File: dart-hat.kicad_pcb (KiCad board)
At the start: 2 copper layers, 85 x 56 mm, 119 parts, among them IC1 PCA9615DPJ, J0 XT60 Female, J1 Raspberry_Pi_2_3, J2 CAN_CON, J3 SM07B-SRSS-TBLFSN, M1 Motor_Servo, M2 Motor_Servo, M3 Motor_Servo, M4 Motor_Servo, Q1 Q_PMOS_DSG, Q2 Q_PMOS_DSG, Q3 DMMT5401, U1 CAT24C32YI-GT3, U2 MCP2515-xSO, U3 MCP2551-I-SN, U4 LM2677S-5.0, U5 BMI088, U6 PCA9685PW, U7 LM2677S-5.0, U8 LM2677S-3.3, Y1 16MHz

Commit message: [schematic] fix 3v3 symbol pin to use 3v3_pi instead of 5V_SRV
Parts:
- C10, C19, C2, C20, C3, C9, IC1, JP1, JP4, JP6, R15, R16, R18, R19, R20, R21, R22, R4, R5, R6, R7, R8, U1, U6: moved to B.Cu
- CP1, CP21: value 1000uF -> 330uF; footprint EEE-TP1J102M:CAP_EEETP1J102M -> Capacitor_THT:CP_Radial_D10.0mm_P5.00mm
- D5: value D_Schottky -> D_Schottky_KKA
- Q2: footprint Package_TO_SOT_SMD:TO-263-3_TabPin2 -> Package_SO:SOIC-8-1EP_3.9x4.9mm_P1.27mm_EP2.29x3mm
- moved C23 230.6 mm to (34.0, 140.4), turned to 90 degrees
- moved C22 215.1 mm to (27.0, 140.5), turned to 90 degrees
- moved C24 211.4 mm to (41.0, 140.4), turned to 90 degrees
- moved C5 205.8 mm to (131.1, 188.3), turned to 270 degrees
- moved U7 203.7 mm to (51.2, 143.6)
- moved TP5 199.6 mm to (124.0, 176.0)
- moved TP6 198.6 mm to (124.0, 179.0)
- moved C4 196.5 mm to (131.1, 183.3), turned to 270 degrees
- moved C7 190.1 mm to (141.2, 173.3), turned to 90 degrees
- moved C25 188.4 mm to (51.7, 131.8)
- moved C26 185.8 mm to (76.0, 133.0), turned to 90 degrees
- moved JP2 182.4 mm to (138.0, 165.3)
- moved C27 179.0 mm to (83.0, 133.0), turned to 90 degrees
- moved D6 179.0 mm to (67.0, 149.0), turned to 90 degrees
- moved C12 177.7 mm to (25.9, 107.1), turned to 90 degrees
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- renumbered TP0 to TP66
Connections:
- C17 pad 1: +5V_SRV -> +3V3_PI
- C18 pad 1: +5V_SRV -> +3V3_PI
- C2 pad 1: +5V_SRV -> +3V3_PI
- C3 pad 1: +5V_SRV -> +3V3_PI
- D4 pad 2: +3V3 -> /Servo Driver/5V_IN
- D5 pad 1: /Servo Driver/5V_IN -> Net-(D5-Pad1)
- D5 pad 3: (no net) -> GND
- J1 pad 1: +5V_SRV -> +3V3_PI
- J1 pad 17: +5V_SRV -> +3V3_PI
- J3 pad 1: /differential i2c iface/SCL+ -> /differential i2c iface/SCL-
- J3 pad 2: /differential i2c iface/SCL- -> /differential i2c iface/SCL+
- R10 pad 2: +5V_SRV -> +3V3_PI
- R11 pad 2: +5V_SRV -> +3V3_PI
- R4 pad 1: +5V_SRV -> +3V3_PI
- R5 pad 1: +5V_SRV -> +3V3_PI
- R6 pad 1: +5V_SRV -> +3V3_PI
- R7 pad 1: +5V_SRV -> +3V3_PI
- R8 pad 1: +5V_SRV -> +3V3_PI
- R9 pad 2: +5V_SRV -> +3V3_PI
- U1 pad 8: +5V_SRV -> +3V3_PI
- U5 pad 11: +5V_SRV -> +3V3_PI
- U5 pad 3: +5V_SRV -> +3V3_PI
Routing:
- net GND: track 0.00 -> 132.4 mm
- net +BATT: track 0.00 -> 57.7 mm
- net +3V3: track 0.00 -> 31.9 mm
- net +3V3_PI: track 0.00 -> 22.5 mm
- net /Can Interface/CAN_L: track 0.00 -> 17.1 mm
- net /Servo Driver/5V_IN: track 0.00 -> 15.3 mm
- net /LED0: track 0.00 -> 11.3 mm
- net Net-(D2-Pad2): track 0.00 -> 10.5 mm
- net +5V: track 0.00 -> 10.3 mm
- net Net-(C5-Pad2): track 0.00 -> 10.2 mm
- net Net-(C4-Pad1): track 0.00 -> 10.0 mm
- net Net-(Q2-Pad3): track 0.00 -> 10.0 mm
- net /BMI_INT: track 0.00 -> 9.65 mm
- net /Can Interface/CAN_H: track 0.00 -> 9.38 mm
- net Net-(JP2-Pad1): track 0.00 -> 8.11 mm
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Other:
- board size 85 x 56 mm -> 56 x 85 mm
- net class 40V added: clearance 0.6, trace_width 0.25, via_dia 0.6, via_drill 0.4
- board text removed: "Camera Flex Slot (Optional)"
- board text removed: "Dimensions taken from https://github.com/raspberrypi/hats/blob/master/hat-board-mechanical.pdf"
- board text removed: "Select one of these board edges depending upon the type of socket that is used."

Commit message: power supply overhaul
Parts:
- removed the C11 at (41.1, 107.0)
- removed the C12 at (25.9, 107.1)
- removed the C13 at (33.5, 107.0)
- removed the C14 at (52.8, 97.5)
- removed the C15 at (75.8, 97.6)
- removed the C16 at (83.0, 97.8)
- removed CP21: 330uF, Capacitor_THT:CP_Radial_D10.0mm_P5.00mm
- removed the D3 at (67.0, 114.3)
- removed the D6 at (67.0, 149.0)
- removed L2: 22uH, Inductor_SMD:L_10.4x10.4_H4.8
- removed L3: 15uH, DR127-150-R:INDM125125X800N
- removed the R14 at (130.7, 172.0)
- removed the TP5 at (124.0, 176.0)
- removed the TP6 at (124.0, 179.0)
- removed the U4 at (51.8, 108.5)
- removed U8: LM2677S-3.3, LM2677S-3v3:TO127P1435X464-8N
- added C17: 10uF, Capacitor_SMD:C_0603_1608Metric_Pad1.05x0.95mm_HandSolder, F.Cu at (26.9, 192.6)
- added C18: 2.2uF, Capacitor_SMD:C_1210_3225Metric_Pad1.42x2.65mm_HandSolder, F.Cu at (-3.00, 119.5)
- added C19: 2.2uF, Capacitor_SMD:C_1210_3225Metric_Pad1.42x2.65mm_HandSolder, F.Cu at (9.80, 119.5)
- added C20: 2.2uF, Capacitor_SMD:C_1210_3225Metric_Pad1.42x2.65mm_HandSolder, F.Cu at (6.60, 119.5)
- added C21: 2.2uF, Capacitor_SMD:C_1210_3225Metric_Pad1.42x2.65mm_HandSolder, F.Cu at (3.40, 119.5)
- added C36: 0.1uF, Capacitor_SMD:C_0805_2012Metric_Pad1.15x1.40mm_HandSolder, F.Cu at (84.6, 136.7)
- added C37: 10uF, Capacitor_SMD:C_0603_1608Metric_Pad1.05x0.95mm_HandSolder, F.Cu at (26.9, 190.1)
- added C7: 0.1uF, Capacitor_SMD:C_0603_1608Metric_Pad1.05x0.95mm_HandSolder, F.Cu at (159.6, 191.8)
- added C8: 0.1uF, Capacitor_SMD:C_0603_1608Metric_Pad1.05x0.95mm_HandSolder, F.Cu at (159.6, 193.8)
- added C9: 1uF, Capacitor_SMD:C_0603_1608Metric_Pad1.05x0.95mm_HandSolder, F.Cu at (159.6, 195.8)
- added CP2: 330uF, Capacitor_THT:CP_Radial_D10.0mm_P5.00mm, F.Cu at (53.0, 26.5)
- added CP4: 470uF, Capacitor_SMD:CP_Elec_10x10.5, F.Cu at (67.6, 121.0)
- added D8: Diode_Schottky_Common_Cathode, Package_TO_SOT_SMD:TO-263-2, F.Cu at (52.0, 132.2)
- added Q4: Q_NMOS_DGS, Package_TO_SOT_SMD:TO-263-2, F.Cu at (53.2, 112.2)
- added R24: NU, Resistor_SMD:R_0603_1608Metric_Pad1.05x0.95mm_HandSolder, F.Cu at (17.5, 122.9)
- added R25: 2.36k, Resistor_SMD:R_0603_1608Metric_Pad1.05x0.95mm_HandSolder, F.Cu at (25.2, 113.4)
- added R26: 54.9k, Resistor_SMD:R_0805_2012Metric_Pad1.15x1.40mm_HandSolder, F.Cu at (28.0, 114.6)
- added R27: 24.9k, Resistor_SMD:R_0603_1608Metric_Pad1.05x0.95mm_HandSolder, F.Cu at (22.8, 129.0)
- added R28: 0.01, RL3720WT-R010-F:RESC2037X70N, F.Cu at (41.9, 132.2)
- added R29: 18k, Resistor_SMD:R_0603_1608Metric_Pad1.05x0.95mm_HandSolder, F.Cu at (27.9, 128.6)
- added R30: 5.11, Resistor_SMD:R_2512_6332Metric_Pad1.52x3.35mm_HandSolder, F.Cu at (51.6, 140.0)
- added R31: 10, Resistor_SMD:R_0805_2012Metric_Pad1.15x1.40mm_HandSolder, F.Cu at (85.2, 145.8)
- added R32: 5.11k, Resistor_SMD:R_0603_1608Metric_Pad1.05x0.95mm_HandSolder, F.Cu at (85.1, 143.8)
- added R33: 1.62k, Resistor_SMD:R_0603_1608Metric_Pad1.05x0.95mm_HandSolder, F.Cu at (85.0, 142.1)
- added TP14: TestPoint, TestPoint:TestPoint_Pad_1.0x1.0mm, F.Cu at (20.0, 131.6)
- added U6: IFX27001TFV, Package_TO_SOT_SMD:TO-252-2, F.Cu at (18.7, 192.9)
- C1: renamed from C2; footprint Capacitor_SMD:C_0805_2012Metric_Pad1.15x1.40mm_HandSolder -> Capacitor_SMD:C_0603_1608Metric_Pad1.05x0.95mm_HandSolder
- C10: renamed from C8; footprint Capacitor_SMD:C_0805_2012Metric_Pad1.15x1.40mm_HandSolder -> Capacitor_SMD:C_0603_1608Metric_Pad1.05x0.95mm_HandSolder
- C11: renamed from C9; footprint Capacitor_SMD:C_0805_2012Metric_Pad1.15x1.40mm_HandSolder -> Capacitor_SMD:C_0603_1608Metric_Pad1.05x0.95mm_HandSolder
- C12: renamed from C10; footprint Capacitor_SMD:C_0805_2012Metric_Pad1.15x1.40mm_HandSolder -> Capacitor_SMD:C_0603_1608Metric_Pad1.05x0.95mm_HandSolder
- C13: renamed from C17; footprint Capacitor_SMD:C_0805_2012Metric_Pad1.15x1.40mm_HandSolder -> Capacitor_SMD:C_0603_1608Metric_Pad1.05x0.95mm_HandSolder
- C14: renamed from C18; footprint Capacitor_SMD:C_0805_2012Metric_Pad1.15x1.40mm_HandSolder -> Capacitor_SMD:C_0603_1608Metric_Pad1.05x0.95mm_HandSolder
- C15: renamed from C19; footprint Capacitor_SMD:C_0805_2012Metric_Pad1.15x1.40mm_HandSolder -> Capacitor_SMD:C_0603_1608Metric_Pad1.05x0.95mm_HandSolder
- C16: renamed from C20; footprint Capacitor_SMD:C_0805_2012Metric_Pad1.15x1.40mm_HandSolder -> Capacitor_SMD:C_0603_1608Metric_Pad1.05x0.95mm_HandSolder
- C2: renamed from C3; footprint Capacitor_SMD:C_0805_2012Metric_Pad1.15x1.40mm_HandSolder -> Capacitor_SMD:C_0603_1608Metric_Pad1.05x0.95mm_HandSolder
- C22: value 15uF -> 270pF; footprint Capacitor_Tantalum_SMD:CP_EIA-7260-15_AVX-R_Pad2.68x6.30mm_HandSolder -> Capacitor_SMD:C_0603_1608Metric_Pad1.05x0.95mm_HandSolder
- C23: value 15uF -> 2.2uF; footprint Capacitor_Tantalum_SMD:CP_EIA-7260-15_AVX-R_Pad2.68x6.30mm_HandSolder -> Capacitor_SMD:C_1210_3225Metric_Pad1.42x2.65mm_HandSolder
- C24: value 15uF -> 0.022uF; footprint Capacitor_Tantalum_SMD:CP_EIA-7260-15_AVX-R_Pad2.68x6.30mm_HandSolder -> Capacitor_SMD:C_0603_1608Metric_Pad1.05x0.95mm_HandSolder
- C25: value 0.01uF -> NU; footprint Capacitor_SMD:C_0805_2012Metric_Pad1.15x1.40mm_HandSolder -> Capacitor_SMD:C_0603_1608Metric_Pad1.05x0.95mm_HandSolder
- C26: value 180uF -> 100pF; footprint Capacitor_Tantalum_SMD:CP_EIA-7260-38_AVX-R_Pad2.68x6.30mm_HandSolder -> Capacitor_SMD:C_0603_1608Metric_Pad1.05x0.95mm_HandSolder
- C27: value 180uF -> 0.022uF; footprint Capacitor_Tantalum_SMD:CP_EIA-7260-38_AVX-R_Pad2.68x6.30mm_HandSolder -> Capacitor_SMD:C_0603_1608Metric_Pad1.05x0.95mm_HandSolder
- C28: value 15uF -> 0.1uF; footprint Capacitor_Tantalum_SMD:CP_EIA-7260-38_AVX-R_Pad2.68x6.30mm_HandSolder -> Capacitor_SMD:C_0805_2012Metric_Pad1.15x1.40mm_HandSolder
- C29: value 15uF -> 1uF; footprint Capacitor_Tantalum_SMD:CP_EIA-7260-38_AVX-R_Pad2.68x6.30mm_HandSolder -> Capacitor_SMD:C_0603_1608Metric_Pad1.05x0.95mm_HandSolder
- C3: renamed from C4; footprint Capacitor_SMD:C_0805_2012Metric_Pad1.15x1.40mm_HandSolder -> Capacitor_SMD:C_0603_1608Metric_Pad1.05x0.95mm_HandSolder
- C30: value 15uF -> 0.1uF; footprint Capacitor_Tantalum_SMD:CP_EIA-7260-38_AVX-R_Pad2.68x6.30mm_HandSolder -> Capacitor_SMD:C_0603_1608Metric_Pad1.05x0.95mm_HandSolder
- C31: value 0.01uF -> 100pF; footprint Capacitor_SMD:C_0805_2012Metric_Pad1.15x1.40mm_HandSolder -> Capacitor_SMD:C_0603_1608Metric_Pad1.05x0.95mm_HandSolder
- C32: value 120uF -> 0.015uF; footprint Capacitor_Tantalum_SMD:CP_EIA-7260-38_AVX-R_Pad2.68x6.30mm_HandSolder -> Capacitor_SMD:C_0402_1005Metric
- C33: value 120uF -> 1000pF; footprint Capacitor_Tantalum_SMD:CP_EIA-7260-38_AVX-R_Pad2.68x6.30mm_HandSolder -> Capacitor_SMD:C_0805_2012Metric_Pad1.15x1.40mm_HandSolder
- C34, C35: value 120uF -> 47uF; footprint Capacitor_Tantalum_SMD:CP_EIA-7260-38_AVX-R_Pad2.68x6.30mm_HandSolder -> Capacitor_SMD:C_1210_3225Metric_Pad1.42x2.65mm_HandSolder
- C4: renamed from C5; footprint Capacitor_SMD:C_0805_2012Metric_Pad1.15x1.40mm_HandSolder -> Capacitor_SMD:C_0603_1608Metric_Pad1.05x0.95mm_HandSolder
- C5: renamed from C6; footprint Capacitor_SMD:C_0805_2012Metric_Pad1.15x1.40mm_HandSolder -> Capacitor_SMD:C_0603_1608Metric_Pad1.05x0.95mm_HandSolder
- C6: renamed from C7; footprint Capacitor_SMD:C_0805_2012Metric_Pad1.15x1.40mm_HandSolder -> Capacitor_SMD:C_0603_1608Metric_Pad1.05x0.95mm_HandSolder
- D1: renamed from D2; footprint Diode_SMD:D_SOD-523 -> Diode_SMD:D_SOT-23_ANK
- D4: renamed from D1; footprint Package_TO_SOT_THT:TO-220-2_Horizontal_TabUp -> Diode_SMD:D_SOD-128
- D6: renamed from D5; footprint TO254P1521X483-4N:TO254P1521X483-4N -> Diode_SMD:D_SOD-128
- D7: value D_Schottky -> NU; footprint TO254P1521X483-4N:TO254P1521X483-4N -> Diode_SMD:D_SOD-128
- F1: footprint Fuse:Fuse_0805_2012Metric_Pad1.15x1.40mm_HandSolder -> Fuse:Fuse_Bourns_MF-SM_7.98x5.44mm
- L1: value 22uH -> 6.8uH; footprint Inductor_SMD:L_10.4x10.4_H4.8 -> Inductor_SMD:L_12x12mm_H8mm
- Q1: footprint Package_TO_SOT_SMD:TO-263-3_TabPin2 -> Package_TO_SOT_SMD:TO-263-2
- Q2: footprint Package_SO:SOIC-8-1EP_3.9x4.9mm_P1.27mm_EP2.29x3mm -> Package_TO_SOT_SMD:TO-263-2
- R1, R2, R3: footprint Resistor_SMD:R_0805_2012Metric_Pad1.15x1.40mm_HandSolder -> Resistor_SMD:R_0603_1608Metric_Pad1.05x0.95mm_HandSolder
- R10: renamed from R8; footprint Resistor_SMD:R_0805_2012Metric_Pad1.15x1.40mm_HandSolder -> Resistor_SMD:R_0402_1005Metric
- R15: renamed from R13; footprint Resistor_SMD:R_0805_2012Metric_Pad1.15x1.40mm_HandSolder -> Resistor_SMD:R_0603_1608Metric_Pad1.05x0.95mm_HandSolder
- R18: renamed from R17; value 120 -> 150
- R20: renamed from R19; footprint Resistor_SMD:R_0805_2012Metric_Pad1.15x1.40mm_HandSolder -> Resistor_SMD:R_1206_3216Metric_Pad1.42x1.75mm_HandSolder
- R21: renamed from R20; footprint Resistor_SMD:R_0805_2012Metric_Pad1.15x1.40mm_HandSolder -> Resistor_SMD:R_1206_3216Metric_Pad1.42x1.75mm_HandSolder
- R22: renamed from R21; footprint Resistor_SMD:R_0805_2012Metric_Pad1.15x1.40mm_HandSolder -> Resistor_SMD:R_1206_3216Metric_Pad1.42x1.75mm_HandSolder
- R23: renamed from R22; footprint Resistor_SMD:R_0805_2012Metric_Pad1.15x1.40mm_HandSolder -> Resistor_SMD:R_1206_3216Metric_Pad1.42x1.75mm_HandSolder
- R5: renamed from R24; value 120 -> 62; footprint Resistor_SMD:R_0805_2012Metric_Pad1.15x1.40mm_HandSolder -> Resistor_SMD:R_1206_3216Metric_Pad1.42x1.75mm_HandSolder
- R6: renamed from R4; footprint Resistor_SMD:R_0805_2012Metric_Pad1.15x1.40mm_HandSolder -> Resistor_SMD:R_0603_1608Metric_Pad1.05x0.95mm_HandSolder
- R7: renamed from R5; footprint Resistor_SMD:R_0805_2012Metric_Pad1.15x1.40mm_HandSolder -> Resistor_SMD:R_0603_1608Metric_Pad1.05x0.95mm_HandSolder
- TP1: renamed from TP66; footprint TestPoint:TestPoint_Pad_D2.5mm -> TestPoint:TestPoint_Pad_D1.0mm
- TP10: renamed from TP9; footprint TestPoint:TestPoint_Pad_D2.5mm -> TestPoint:TestPoint_Pad_D1.0mm
- TP11: renamed from TP10; footprint TestPoint:TestPoint_Pad_D2.5mm -> TestPoint:TestPoint_Pad_D1.0mm
- TP12: renamed from TP11; footprint TestPoint:TestPoint_Pad_D2.5mm -> TestPoint:TestPoint_Pad_D1.0mm
- TP13: renamed from TP12; footprint TestPoint:TestPoint_Pad_D2.5mm -> TestPoint:TestPoint_Pad_D1.0mm
- TP2: renamed from TP1; footprint TestPoint:TestPoint_Pad_D2.5mm -> TestPoint:TestPoint_Pad_D1.0mm
- TP3: renamed from TP2; footprint TestPoint:TestPoint_Pad_D2.5mm -> TestPoint:TestPoint_Pad_D1.0mm
- TP4: renamed from TP3; footprint TestPoint:TestPoint_Pad_D2.5mm -> TestPoint:TestPoint_Pad_D1.0mm
- TP5: renamed from TP4; footprint TestPoint:TestPoint_Pad_D2.5mm -> TestPoint:TestPoint_Pad_D1.0mm
- TP6: renamed from TP13; footprint TestPoint:TestPoint_Pad_D2.5mm -> TestPoint:TestPoint_Pad_D1.0mm
- TP7: renamed from TP14; footprint TestPoint:TestPoint_Pad_D2.5mm -> TestPoint:TestPoint_Pad_D1.0mm
- TP8: renamed from TP7; footprint TestPoint:TestPoint_Pad_D2.5mm -> TestPoint:TestPoint_Pad_D1.0mm
- TP9: renamed from TP8; footprint TestPoint:TestPoint_Pad_D2.5mm -> TestPoint:TestPoint_Pad_D1.0mm
- U2: footprint Package_SO:SOIC-18W_7.5x11.6mm_P1.27mm -> MCP2515-IST:SOP65P640X110-20N
- U3: value MCP2551-I-SN -> MCP2562-H-MF; footprint Package_SO:SOIC-8_3.9x4.9mm_P1.27mm -> MCP2562T-E_SN:SOIC127P600X175-8N
- U7: value LM2677S-5.0 -> LM25088MH-2; footprint LM2677S-5:TO127P1435X464-8N -> SOP65P640X120-17N
- moved C32 66.6 mm to (30.7, 128.4), turned to 180 degrees
- moved C26 55.9 mm to (20.3, 128.0), turned to 0 degrees
- moved C28 55.1 mm to (30.8, 113.6), turned to 180 degrees
- moved C33 54.2 mm to (45.6, 139.0), turned to 0 degrees
- moved C29 51.8 mm to (38.2, 116.9)
- moved C30 49.6 mm to (42.2, 118.9)
- moved C27 43.4 mm to (40.8, 122.8), turned to 270 degrees
- moved D7 40.6 mm to (65.6, 144.8), turned to 0 degrees
- moved C31 40.3 mm to (31.5, 130.8), turned to 180 degrees
- moved C23 39.8 mm to (0.20, 119.5), turned to 270 degrees
- moved C34 39.1 mm to (84.6, 130.7), turned to 0 degrees
- moved L1 34.4 mm to (68.5, 133.2), turned to 0 degrees
- moved C35 33.8 mm to (84.7, 133.9), turned to 0 degrees
- moved C25 33.2 mm to (25.2, 111.8), turned to 180 degrees
- moved U7 29.8 mm to (33.0, 120.0)
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- renumbered D8 to D2, D9 to D3, D4 to D5, J0 to J1, J1 to J2, J2 to J3, J3 to J4, R9 to R11, R10 to R12, R11 to R13, R12 to R14, R15 to R16, R16 to R17, R18 to R19, R23 to R4, R6 to R8, R7 to R9, U5 to U4, U6 to U5
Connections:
- C22 pad 1: +BATT -> Net-(C22-Pad1)
- C24 pad 1: +BATT -> Net-(C24-Pad1)
- C25 pad 2: Net-(C25-Pad2) -> GND
- C26 pad 1: +5V_SRV -> Net-(C26-Pad1)
- C26 pad 2: GND -> Net-(C26-Pad2)
- C27 pad 1: +5V_SRV -> Net-(C27-Pad1)
- C28 pad 1: +BATT -> GND
- C28 pad 2: GND -> +BATT
- C29 pad 1: +BATT -> /5V Power Supply/Vcc
- C30 pad 1: +BATT -> Net-(C30-Pad1)
- C30 pad 2: GND -> Net-(C30-Pad2)
- C32 pad 1: +3V3 -> Net-(C32-Pad1)
- C32 pad 2: GND -> Net-(C31-Pad2)
- C33 pad 1: +3V3 -> Net-(C33-Pad1)
- C33 pad 2: GND -> Net-(C33-Pad2)
- C34 pad 1: +3V3 -> /5V Power Supply/VOUT
- C35 pad 1: +3V3 -> /5V Power Supply/VOUT
- D7 pad 1: Net-(C31-Pad1) -> /5V Power Supply/Vcc
- F1 pad 1: +5V_SRV -> +5V
- L1 pad 1: Net-(C14-Pad1) -> Net-(C30-Pad1)
- L1 pad 2: /BEC (pi)/V_OUT -> /5V Power Supply/VOUT
- Q2 pad 1: /BEC (pi)/V_OUT -> /5V Power Supply/VOUT
- Q3 pad 6: /BEC (pi)/V_OUT -> /5V Power Supply/VOUT
- TP4 pad 1: +5V_SRV -> +5V
- U2 pad 1: Net-(TP6-Pad1) -> Net-(U2-Pad1)
- U2 pad 2: Net-(TP5-Pad1) -> Net-(U2-Pad2)
- U3 pad 1: Net-(TP5-Pad1) -> Net-(U2-Pad1)
- U3 pad 3: +3V3 -> +5V
- U3 pad 4: Net-(TP6-Pad1) -> Net-(U2-Pad2)
- U3 pad 5: Net-(U3-Pad5) -> +3V3
- U3 pad 8: Net-(R14-Pad1) -> GND
- U7 pad 1: Net-(C25-Pad1) -> +BATT
- U7 pad 2: +BATT -> Net-(C25-Pad1)
- U7 pad 3: Net-(C25-Pad2) -> Net-(C24-Pad1)
- U7 pad 4: GND -> Net-(C22-Pad1)
- U7 pad 5: Net-(U7-Pad5) -> Net-(C26-Pad1)
- U7 pad 6: +5V_SRV -> GND
- U7 pad 7: Net-(U7-Pad7) -> Net-(C31-Pad2)
- U7 pad 8: GND -> Net-(C31-Pad1)
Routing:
- net +BATT: track 57.7 -> 0.00 mm
- net GND: track 132.4 -> 92.8 mm
- net Net-(D1-Pad2): track 10.5 -> 0.00 mm
- net Net-(Q2-Pad3): track 10.0 -> 0.00 mm
- net Net-(J1-Pad1): track 7.87 -> 0.08 mm
- net +5V: track 10.3 -> 2.54 mm
- net /BEC (pi)/V_OUT: track 7.67 -> 0.00 mm
- net Net-(Q3-Pad1): track 3.90 -> 0.00 mm

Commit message: [pcb] added copper planes
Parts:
- removed TP1, TP10, TP11, TP12, TP13, TP2, TP3, TP4, TP5, TP6, TP7, TP8, TP9: TestPoint, TestPoint:TestPoint_Pad_D1.0mm
- added ?: , RPi_Hat:RPi_Hat_Mounting_Hole, F.Cu at (155.5, 58.2)
- added ?: , RPi_Hat:RPi_Hat_Mounting_Hole, F.Cu at (106.5, 58.2)
- added ?: , RPi_Hat:RPi_Hat_Mounting_Hole, F.Cu at (106.5, 116.2)
- added ?: , RPi_Hat:RPi_Hat_Mounting_Hole, F.Cu at (155.5, 116.2)
- added J2: Raspberry_Pi_2_3, Connector_PinHeader_2.54mm:PinHeader_2x20_P2.54mm_Vertical, F.Cu at (154.2, 63.1)
- added REF**: PinHeader_2x02_P2.54mm_Vertical, Connector_PinHeader_2.54mm:PinHeader_2x02_P2.54mm_Vertical, F.Cu at (105.2, 108.8)
- added REF**: PinHeader_2x02_P2.54mm_Vertical, Connector_PinHeader_2.54mm:PinHeader_2x02_P2.54mm_Vertical, F.Cu at (148.1, 56.9)
- added REF**: PinHeader_2x02_P2.54mm_Vertical, Connector_PinHeader_2.54mm:PinHeader_2x02_P2.54mm_Vertical, F.Cu at (178.8, 56.9)
- added REF**: PinHeader_2x02_P2.54mm_Vertical, Connector_PinHeader_2.54mm:PinHeader_2x02_P2.54mm_Vertical, F.Cu at (221.6, 108.8)
- ? (x4), C10, C13, C14, C17, C25, C27, C30, C31, C32, C37, C5, C6, C7, C8, C9, D2, D3, D5, D6, F1, J2, J4, JP2, JP5, JP7, R11, R12, R13, R14, R15, R18, R24, R29, R4, R5, U2, U4, U6, Y1: moved to B.Cu
- C1, C2, JP1, R10, R6, R7, U1: moved to F.Cu
- CP1: value 330uF -> 470uF; footprint Capacitor_THT:CP_Radial_D10.0mm_P5.00mm -> Capacitor_SMD:CP_Elec_10x10.5
- CP2: value 330uF -> 470uF; footprint Capacitor_THT:CP_Radial_D10.0mm_P5.00mm -> Capacitor_SMD:CP_Elec_10x10.5; moved to B.Cu
- D8: footprint Package_TO_SOT_SMD:TO-263-2 -> PMEG045V150EPDZ:NEXPERIA_PMEG045V150EPDZ
- J3: footprint JST-PH-S4B-K-S-LF-SN:JST_S4B-PH-K-S(LF)(SN) -> Connector_JST:JST_PH_S4B-PH-SM4-TB_1x04-1MP_P2.00mm_Horizontal; moved to B.Cu
- L1: footprint Inductor_SMD:L_12x12mm_H8mm -> SRP6060FA:L_6.3x6.3_H3
- Q1, Q2: value Q_PMOS_DSG -> SI7611DN-T1-GE3; footprint Package_TO_SOT_SMD:TO-263-2 -> SI7611DN-T1-GE3:VISHAY_SIS468DN-T1-GE3
- Q4: value Q_NMOS_DGS -> Q_NMOS_SGD; footprint Package_TO_SOT_SMD:TO-263-2 -> CSD18511Q5AT:CSD18511Q5AT
- U3: value MCP2562-H-MF -> MCP2562-H-P; moved to B.Cu
- moved U6 233.6 mm to (209.8, 58.5)
- moved C37 223.6 mm to (211.0, 63.1), turned to 180 degrees
- moved C17 221.3 mm to (203.0, 58.7), turned to 270 degrees
- moved CP2 178.4 mm to (214.0, 103.4), turned to 0 degrees
- moved F1 166.4 mm to (210.8, 114.3), turned to 90 degrees
- moved R18 162.5 mm to (189.3, 117.7), turned to 180 degrees
- moved D6 159.9 mm to (206.0, 115.6), turned to 270 degrees
- moved D5 158.3 mm to (189.3, 115.8)
- moved R20 157.2 mm to (202.5, 108.2), turned to 90 degrees
- moved R21 155.8 mm to (199.9, 108.2), turned to 90 degrees
- moved R22 154.6 mm to (197.4, 108.2), turned to 90 degrees
- moved R23 153.4 mm to (194.8, 108.2), turned to 90 degrees
- moved C16 148.0 mm to (206.5, 100.4), turned to 0 degrees
- moved U5 146.7 mm to (198.5, 101.8), turned to 90 degrees
- moved C15 145.5 mm to (206.5, 98.8), turned to 0 degrees
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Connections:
- D8 pad 2: Net-(C30-Pad1) -> Net-(C33-Pad1)
- Q1 pad 1: Net-(J1-Pad1) -> +BATT
- Q1 pad 3: Net-(D1-Pad2) -> +BATT
- Q2 pad 1: /5V Power Supply/VOUT -> +5V
- Q2 pad 3: Net-(Q2-Pad3) -> +5V
- Q3 pad 4: Net-(Q2-Pad3) -> Net-(Q2-Pad4)
- Q4 pad 1: +BATT -> Net-(C30-Pad1)
- Q4 pad 3: Net-(C30-Pad1) -> +BATT
- R3 pad 1: Net-(Q2-Pad3) -> Net-(Q2-Pad4)
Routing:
- net +5V: track 2.54 -> 196.4 mm, vias 0 -> 14
- net +3V3_PI: track 22.5 -> 138.1 mm, vias 0 -> 1
- net +3V3: track 31.9 -> 146.4 mm, vias 0 -> 4
- net Net-(C30-Pad1): track 0.00 -> 76.4 mm, vias 0 -> 2
- net +BATT: track 0.00 -> 71.7 mm
- net /SCLK_CAN: track 0.00 -> 61.5 mm, vias 0 -> 2
- net /SDA: track 2.00 -> 61.6 mm, vias 0 -> 3
- net /SCL: track 2.77 -> 60.7 mm, vias 0 -> 3
- net /5V Power Supply/VOUT: track 0.00 -> 57.2 mm
- net GND: track 92.8 -> 148.5 mm, vias 0 -> 15
- net Net-(Q4-Pad2): track 0.00 -> 49.7 mm, vias 0 -> 2
- net /MISO_CAN: track 0.00 -> 48.9 mm, vias 0 -> 2
- net /MOSI_CAN: track 0.00 -> 47.8 mm, vias 0 -> 2
- net /CS_CAN: track 0.00 -> 45.8 mm, vias 0 -> 2
- net /CS_GYRO: track 0.00 -> 45.6 mm, vias 0 -> 2
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- added copper zone on B.Cu, net +5V
- added copper zone on F.Cu, net +5V
- added copper zone on F.Cu, net +BATT
- added copper zone on F.Cu, net /5V Power Supply/VOUT
- added copper zone on B.Cu, net GND
- added copper zone on F.Cu, net GND
- added copper zone on F.Cu, net Net-(J1-Pad1)
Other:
- board size 56 x 85 mm -> 123.3 x 65 mm
- copper layers 2 -> 4
- net class 40V: clearance 0.6 -> 0.1
- board text added: "put anime grill here"

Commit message: ready?
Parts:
- removed JP4, JP6: Jumper, Connector_PinHeader_2.54mm:PinHeader_1x02_P2.54mm_Vertical
- removed TP14: TestPoint, TestPoint:TestPoint_Pad_1.0x1.0mm
- added REF**: PinHeader_2x02_P2.54mm_Vertical, Connector_PinHeader_2.54mm:PinHeader_2x02_P2.54mm_Vertical, F.Cu at (201.7, 92.5)
- JP1: value Jumper_NO_Small -> WP_EN
- JP3: value Jumper -> CAN_INT
- JP7: value Jumper_NO_Small -> BMI_INT
- moved R18 9.41 mm to (179.9, 117.7)
- moved D3 9.40 mm to (173.3, 103.3)
- moved F1 9.40 mm to (201.4, 114.3)
- moved IC1 9.40 mm to (204.3, 88.8)
- moved J4 9.40 mm to (213.9, 89.7)
- moved JP1 9.40 mm to (177.4, 91.2)
- moved M4 9.40 mm to (185.4, 112.9)
- moved R15 9.40 mm to (193.7, 86.8)
- moved R19 9.40 mm to (188.4, 96.8)
- moved R23 9.40 mm to (185.4, 108.2)
- moved R4 9.40 mm to (178.3, 101.2)
- moved REF** 9.40 mm to (212.2, 108.8)
- moved SHD 9.40 mm to (212.4, 99.0)
- moved ? 9.40 mm to (164.5, 116.2)
- moved ? 9.40 mm to (213.5, 116.2)
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- renumbered JP5 to SHD, JP2 to T_CAN
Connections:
- Q4 pad 1: Net-(C30-Pad1) -> Net-(Q4-Pad2)
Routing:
- net +5V: track 196.4 -> 142.2 mm, vias 14 -> 25
- net GND: track 148.5 -> 131.5 mm, vias 15 -> 419
- net +3V3: track 146.4 -> 153.9 mm, vias 4 -> 11
- net Net-(Q4-Pad2): track 49.7 -> 55.8 mm
- net /5V Power Supply/Vcc: track 32.1 -> 36.7 mm
- net Net-(C26-Pad2): track 3.21 -> 0.00 mm
- net Net-(C30-Pad1): track 76.4 -> 74.1 mm
- net /5V Power Supply/VOUT: track 57.2 -> 55.0 mm
- net Net-(C33-Pad1): track 41.9 -> 40.9 mm
- net Net-(Q2-Pad4): track 6.72 -> 7.19 mm, vias 0 -> 2
- net /MOSI_IMU: vias 1 -> 0
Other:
- board size 123.3 x 65 mm -> 114 x 65 mm
- rule via_min_size: 0.4 -> 0.508
- board text added: "+"
- board text added: "+5v"
- board text added: "-"
- board text added: "1 2 3 4"
- board text added: "@kemfic 2021"
- board text added: "Avionics Module"
- board text added: "DART"
- board text added: "GND"
- board text added: "GND CANL CANH"
- board text added: "PWM + -"
- board text added: "Power Delivery Module"
- board text added: "SCL- SCL+ SDA+ SDA- 3v3 GND SHD"
- board text added: "SDA+|SCL+ SDA-|SCL-"
- board text added: "kemfic 2021"
- board text added: "rev. 1"
- board text removed: "put anime grill here"

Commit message: add mousebites
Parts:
- added mouse-bite-2mm-slot: VAL**, Panelization:mouse-bite-2mm-slot, F.Cu at (160.0, 110.6)
- added mouse-bite-2mm-slot: VAL**, Panelization:mouse-bite-2mm-slot, F.Cu at (160.0, 91.8)
- added mouse-bite-2mm-slot: VAL**, Panelization:mouse-bite-2mm-slot, F.Cu at (160.0, 81.6)
- added mouse-bite-2mm-slot: VAL**, Panelization:mouse-bite-2mm-slot, F.Cu at (160.0, 62.8)
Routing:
- net +5V: track 142.2 -> 150.2 mm
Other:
- outline, holes or cut-outs redrawn

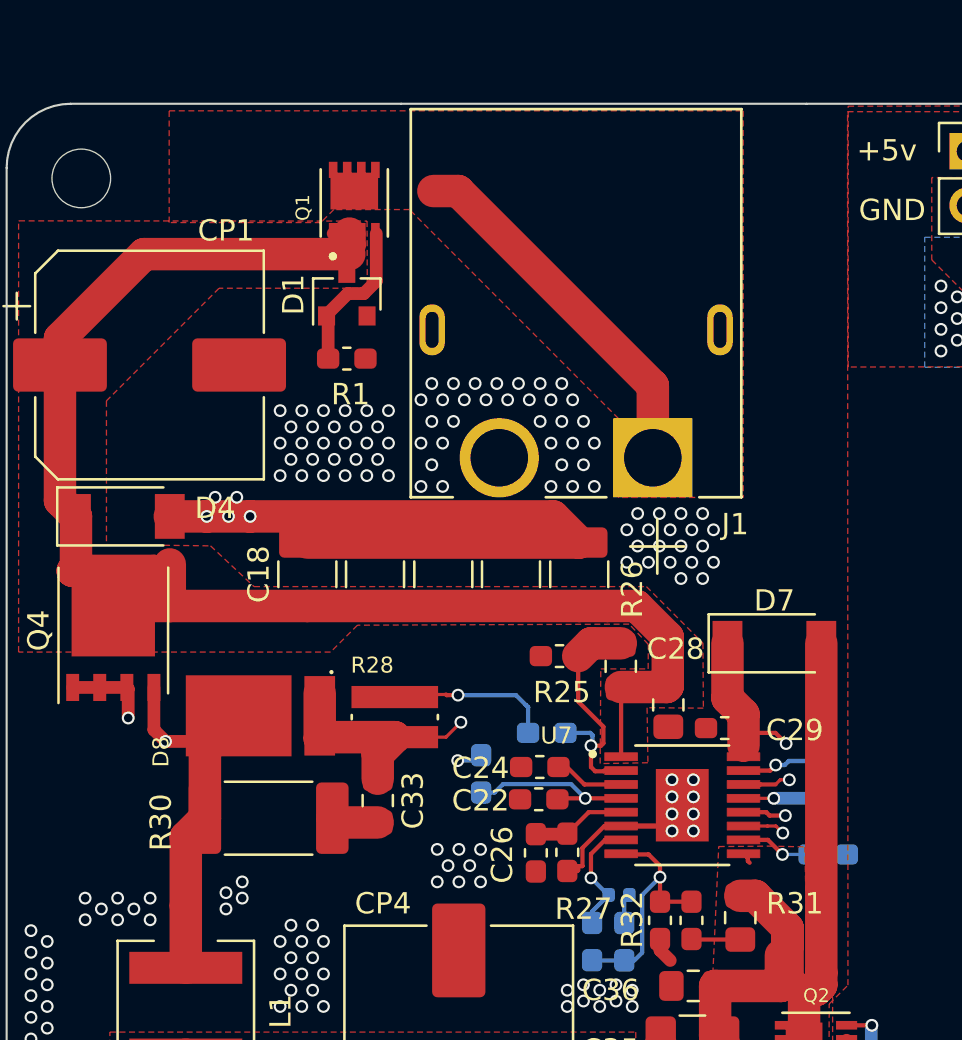
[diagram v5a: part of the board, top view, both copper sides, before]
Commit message: added vias and graphics
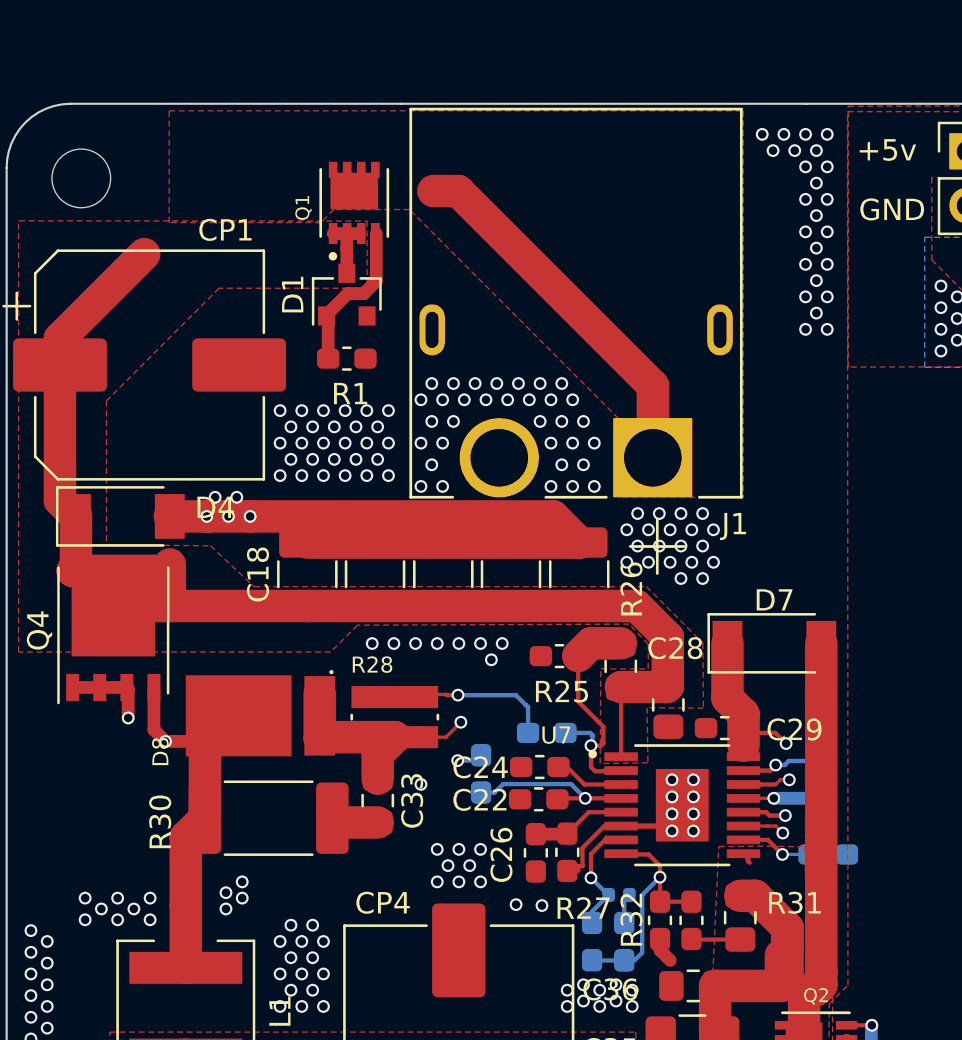
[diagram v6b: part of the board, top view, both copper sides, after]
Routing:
- net +BATT: track 71.7 -> 61.4 mm
- net GND: vias 419 -> 454
